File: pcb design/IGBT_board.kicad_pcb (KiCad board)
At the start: 6 copper layers, 200 x 100 mm, 44 parts, among them Q1 IGBT, Q10 IGBT, Q11 IGBT, Q12 IGBT, Q2 IGBT, Q3 IGBT, Q4 IGBT, Q5 IGBT, Q6 IGBT, Q7 IGBT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

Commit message: Draft of bus bars and mounting points
Signed-off-by: Marcos Chaparro <mchaparro@paltatech.com>
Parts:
- MP1: footprint paltatech:heatsink-watercooled-20x210mm -> heatsink-watercooled-20x210mm
- moved R17 360.5 mm to (25.2, -38.8), turned to 90 degrees
- moved R18 340.0 mm to (29.8, -38.8), turned to 90 degrees
- moved R21 336.3 mm to (47.2, -38.8), turned to 90 degrees
- moved R20 333.9 mm to (40.8, -25.2), turned to 270 degrees
- moved R22 333.7 mm to (51.8, -38.8), turned to 90 degrees
- moved R19 332.0 mm to (36.2, -25.2), turned to 270 degrees
- moved R23 315.3 mm to (58.2, -25.2), turned to 270 degrees
- moved R24 301.6 mm to (62.8, -25.2), turned to 270 degrees
- moved R14 190.4 mm to (3.25, -38.8), turned to 90 degrees
- moved R10 183.5 mm to (-14.2, -38.8), turned to 90 degrees
- moved R1 182.1 mm to (-62.8, -38.8), turned to 90 degrees
- moved R6 180.7 mm to (-36.2, -38.8), turned to 90 degrees
- moved R9 180.7 mm to (-18.8, -38.8), turned to 90 degrees
- moved R13 179.4 mm to (7.75, -38.8), turned to 90 degrees
- moved R5 178.0 mm to (-40.8, -38.8), turned to 90 degrees
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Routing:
- net GATE_LOW: track 0.00 -> 140.9 mm
- net (no net): track 110.8 -> 0.00 mm
- net GATE_HIGH: track 98.0 -> 153.7 mm
- net Net-(Q8-Pad1): track 0.00 -> 11.4 mm
- net Net-(Q6-Pad1): track 0.00 -> 11.4 mm
- net Net-(Q4-Pad1): track 0.00 -> 11.4 mm
- net Net-(Q12-Pad1): track 0.00 -> 11.4 mm
- net Net-(Q11-Pad1): track 0.00 -> 11.4 mm
- net Net-(Q10-Pad1): track 0.00 -> 11.4 mm
- net PHASE: track 10.0 -> 0.00 mm
- net VBUS-: track 9.00 -> 0.00 mm
- net Net-(Q3-Pad1): track 3.54 -> 11.4 mm
- net Net-(Q1-Pad1): track 3.54 -> 11.4 mm
- net Net-(Q7-Pad1): track 4.23 -> 11.4 mm
- net Net-(Q9-Pad1): track 4.31 -> 11.4 mm
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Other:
- board size 200 x 100 mm -> 150 x 100 mm

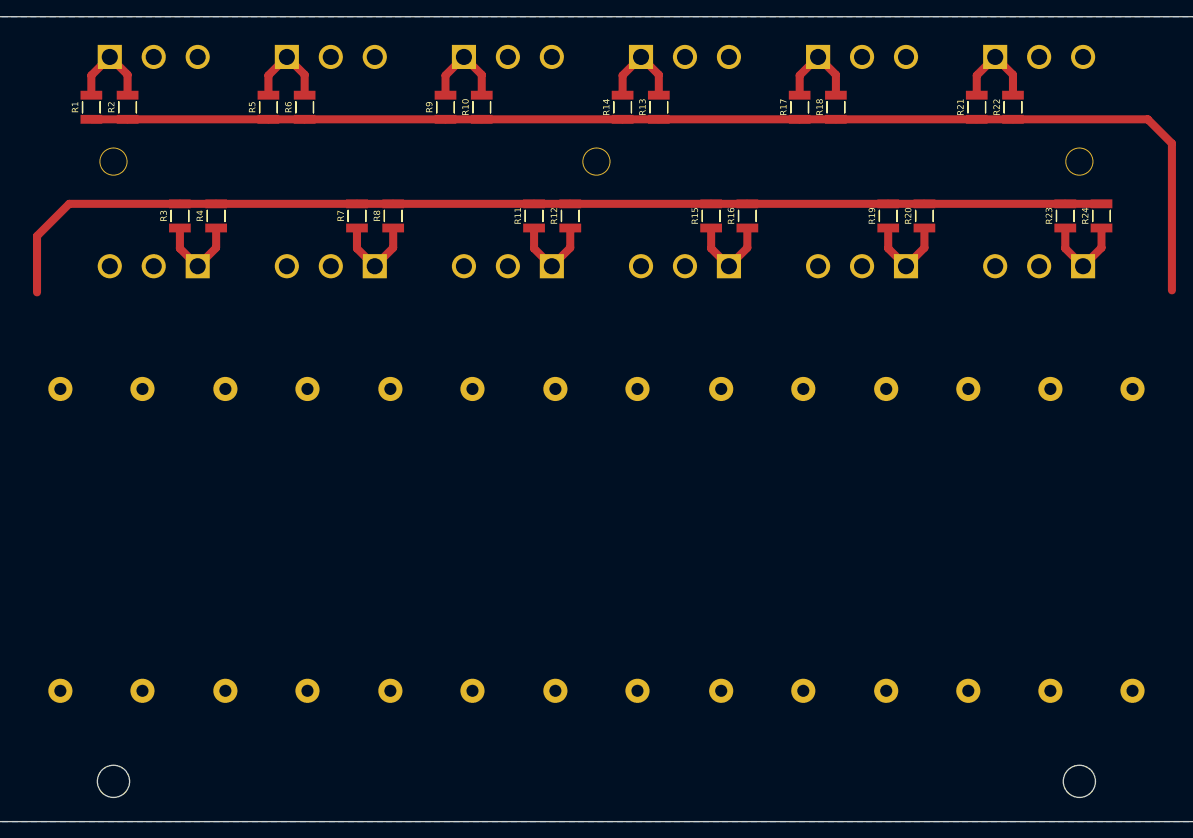
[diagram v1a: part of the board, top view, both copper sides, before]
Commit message: Added IGBT gate driver circuit and isolated power supply
Signed-off-by: Marcos Chaparro <mchaparro@paltatech.com>
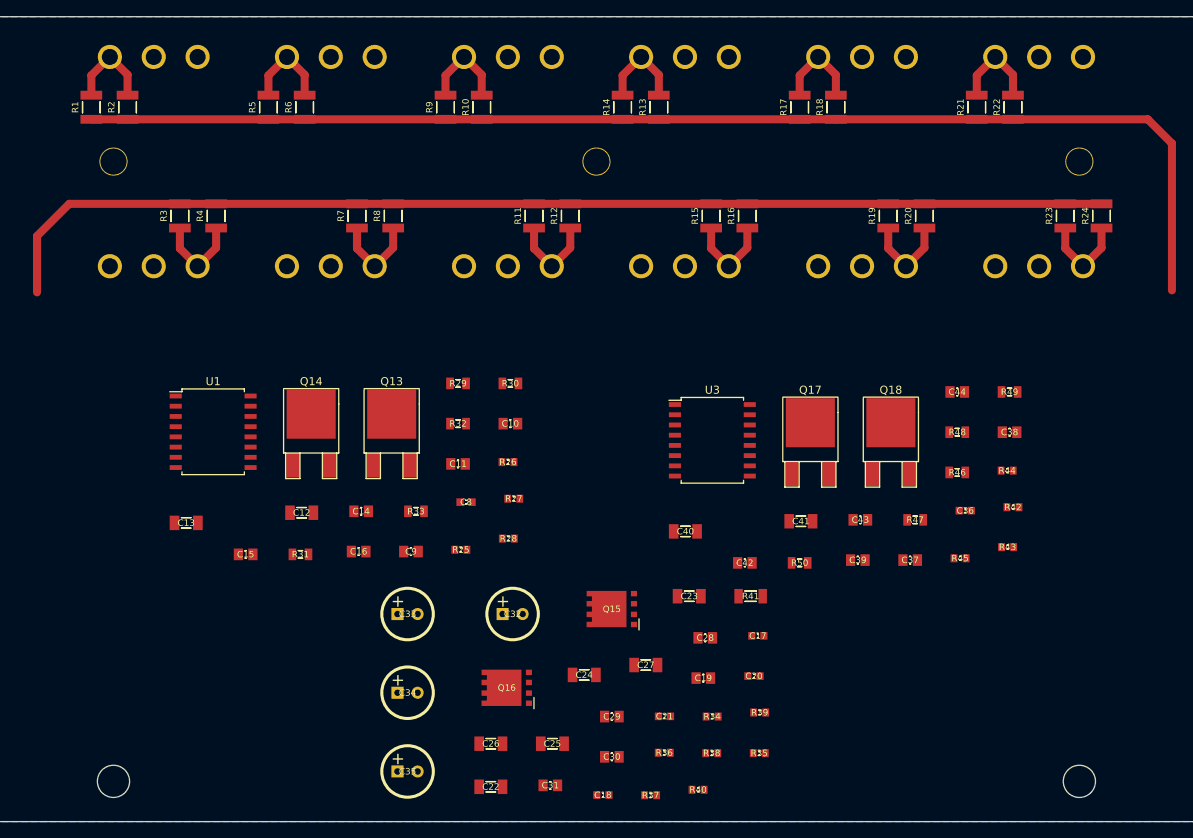
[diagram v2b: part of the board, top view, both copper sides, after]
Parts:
- removed C1, C2, C3, C4, C5, C6, C7: 16uF 700v, paltatech:CAP_FILM_EPCOS_42x20mm
- added C10: 1uF 50v, IPC7351-Nominal:CAPC2012X70, F.Cu at (-10.7, 0.56)
- added C11: 1uF 50v, IPC7351-Nominal:CAPC2012X70, F.Cu at (-17.2, 5.56)
- added C12: 10uF 50v, IPC7351-Nominal:CAPC3216X70, F.Cu at (-36.6, 11.6)
- added C13: 10uF 50v, IPC7351-Nominal:CAPC3216X70, F.Cu at (-51.0, 12.9)
- added C14: 100nF 50v, IPC7351-Nominal:CAPC2012X70, F.Cu at (-29.2, 11.5)
- added C15: 100nF 50v, IPC7351-Nominal:CAPC2012X70, F.Cu at (-43.6, 16.8)
- added C16: 100pF, IPC7351-Nominal:CAPC2012X70, F.Cu at (-29.5, 16.5)
- added C17: 1uF, IPC7351-Nominal:CAPC1608X55, F.Cu at (20.1, 26.9)
- added C18: 22nF, IPC7351-Nominal:CAPC1608X55, F.Cu at (0.80, 46.7)
- added C19: 22uF 16v, IPC7351-Nominal:CAPC2012X70, F.Cu at (13.3, 32.2)
- added C20: 1nF, IPC7351-Nominal:CAPC1608X55, F.Cu at (19.6, 31.9)
- added C21: 470pF, IPC7351-Nominal:CAPC1608X55, F.Cu at (8.45, 36.9)
- added C22: 10uF 50v, IPC7351-Nominal:CAPC3216X70, F.Cu at (-13.1, 45.7)
- added C23: 10uF 50v, IPC7351-Nominal:CAPC3216X70, F.Cu at (11.5, 22.0)
- added C24: 10uF 50v, IPC7351-Nominal:CAPC3216X70, F.Cu at (-1.52, 31.8)
- added C25: 10uF 50v, IPC7351-Nominal:CAPC3216X70, F.Cu at (-5.47, 40.3)
- added C26: 10uF 50v, IPC7351-Nominal:CAPC3216X70, F.Cu at (-13.1, 40.3)
- added C27: 10uF 50v, IPC7351-Nominal:CAPC3216X70, F.Cu at (6.13, 30.5)
- added C28: 100nF 50v, IPC7351-Nominal:CAPC2012X70, F.Cu at (13.5, 27.2)
- added C29: 100nF 50v, IPC7351-Nominal:CAPC2012X70, F.Cu at (1.92, 37.0)
- added C30: 100nF 50v, IPC7351-Nominal:CAPC2012X70, F.Cu at (1.92, 42.0)
- added C31: 100nF 50v, IPC7351-Nominal:CAPC2012X70, F.Cu at (-5.73, 45.5)
- added C32: C-ALUM-6.3mm, pth-passive:C-ALUM-6.3mm, F.Cu at (-10.4, 24.2)
- added C33: C-ALUM-6.3mm, pth-passive:C-ALUM-6.3mm, F.Cu at (-23.5, 24.2)
- added C34: C-ALUM-6.3mm, pth-passive:C-ALUM-6.3mm, F.Cu at (-23.5, 34.0)
- added C35: C-ALUM-6.3mm, pth-passive:C-ALUM-6.3mm, F.Cu at (-23.5, 43.8)
- added C36: 100nF, IPC7351-Nominal:CAPC1608X55, F.Cu at (45.8, 11.4)
- added C37: 1uF 50v, IPC7351-Nominal:CAPC2012X70, F.Cu at (39.0, 17.5)
- added C38: 1uF 50v, IPC7351-Nominal:CAPC2012X70, F.Cu at (51.3, 1.62)
- added C39: 1uF 50v, IPC7351-Nominal:CAPC2012X70, F.Cu at (32.5, 17.5)
- added C40: 10uF 50v, IPC7351-Nominal:CAPC3216X70, F.Cu at (11.1, 13.9)
- added C41: 10uF 50v, IPC7351-Nominal:CAPC3216X70, F.Cu at (25.4, 12.7)
- added C42: 100nF 50v, IPC7351-Nominal:CAPC2012X70, F.Cu at (18.4, 17.9)
- added C43: 100nF 50v, IPC7351-Nominal:CAPC2012X70, F.Cu at (32.8, 12.5)
- added C44: 100pF, IPC7351-Nominal:CAPC2012X70, F.Cu at (44.8, -3.38)
- added C8: 100nF, IPC7351-Nominal:CAPC1608X55, F.Cu at (-16.2, 10.3)
- added C9: 1uF 50v, IPC7351-Nominal:CAPC2012X70, F.Cu at (-23.0, 16.5)
- added Q13: NPN, SMD_Packages:DPAK-2, F.Cu at (-25.4, 5.73)
- added Q14: PNP, SMD_Packages:DPAK-2, F.Cu at (-35.4, 5.73)
- added Q15: CSD19533Q5A, manuf:TEXAS-Q5A, F.Cu at (1.91, 23.6)
- added Q16: CSD19533Q5A, manuf:TEXAS-Q5A, F.Cu at (-11.1, 33.4)
- added Q17: NPN, SMD_Packages:DPAK-2, F.Cu at (26.6, 6.79)
- added Q18: PNP, SMD_Packages:DPAK-2, F.Cu at (36.6, 6.79)
- added R25: 10k, IPC7351-Nominal:RESC1608X50, F.Cu at (-16.8, 16.2)
- added R26: 10k, IPC7351-Nominal:RESC1608X50, F.Cu at (-11.0, 5.34)
- added R27: 10R, IPC7351-Nominal:RESC1608X50, F.Cu at (-10.3, 9.89)
- added R28: 0R, IPC7351-Nominal:RESC1608X50, F.Cu at (-10.9, 14.8)
- added R29: R-0805, IPC7351-Nominal:RESC2012X50, F.Cu at (-17.2, -4.44)
- added R30: R-0805, IPC7351-Nominal:RESC2012X50, F.Cu at (-10.7, -4.44)
- added R31: 10R, IPC7351-Nominal:RESC2012X50, F.Cu at (-36.8, 16.8)
- added R32: 0R, IPC7351-Nominal:RESC2012X50, F.Cu at (-17.2, 0.56)
- added R33: 1k, IPC7351-Nominal:RESC2012X50, F.Cu at (-22.4, 11.5)
- added R34: 0R, IPC7351-Nominal:RESC1608X50, F.Cu at (14.4, 36.9)
- added R35: 26.7k, IPC7351-Nominal:RESC1608X50, F.Cu at (20.2, 41.5)
- added R36: 1k, IPC7351-Nominal:RESC1608X50, F.Cu at (8.43, 41.4)
- added R37: 0R, IPC7351-Nominal:RESC1608X50, F.Cu at (6.73, 46.7)
- added R38: 22R, IPC7351-Nominal:RESC1608X50, F.Cu at (14.3, 41.5)
- added R39: 22R, IPC7351-Nominal:RESC1608X50, F.Cu at (20.3, 36.4)
- added R40: 1.15k, IPC7351-Nominal:RESC1608X50, F.Cu at (12.6, 46.0)
- added R41: 0.22R, IPC7351-Nominal:RESC3216X60, F.Cu at (19.2, 22.0)
- added R42: 10k, IPC7351-Nominal:RESC1608X50, F.Cu at (51.7, 10.9)
- added R43: 10k, IPC7351-Nominal:RESC1608X50, F.Cu at (51.1, 15.9)
- added R44: 10R, IPC7351-Nominal:RESC1608X50, F.Cu at (51.0, 6.40)
- added R45: 0R, IPC7351-Nominal:RESC1608X50, F.Cu at (45.2, 17.3)
- added R46: R-0805, IPC7351-Nominal:RESC2012X50, F.Cu at (44.8, 6.62)
- added R47: R-0805, IPC7351-Nominal:RESC2012X50, F.Cu at (39.6, 12.5)
- added R48: 10R, IPC7351-Nominal:RESC2012X50, F.Cu at (44.8, 1.62)
- added R49: 0R, IPC7351-Nominal:RESC2012X50, F.Cu at (51.3, -3.38)
- added R50: 1k, IPC7351-Nominal:RESC2012X50, F.Cu at (25.2, 17.9)
- added U1: ISO5852S, Housings_SOIC:SOIC-16_7.5x10.3mm_Pitch1.27mm, F.Cu at (-47.6, 1.57)
- added U3: ISO5852S, Housings_SOIC:SOIC-16_7.5x10.3mm_Pitch1.27mm, F.Cu at (14.4, 2.63)
- MP1: footprint heatsink-watercooled-20x210mm -> paltatech:heatsink-watercooled-20x210mm
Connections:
- Q10 pad 3: VBUS- -> PHASE
- Q12 pad 3: VBUS- -> PHASE
- Q2 pad 3: VBUS- -> PHASE
- Q4 pad 3: VBUS- -> PHASE
- Q6 pad 3: VBUS- -> PHASE
- Q8 pad 3: VBUS- -> PHASE

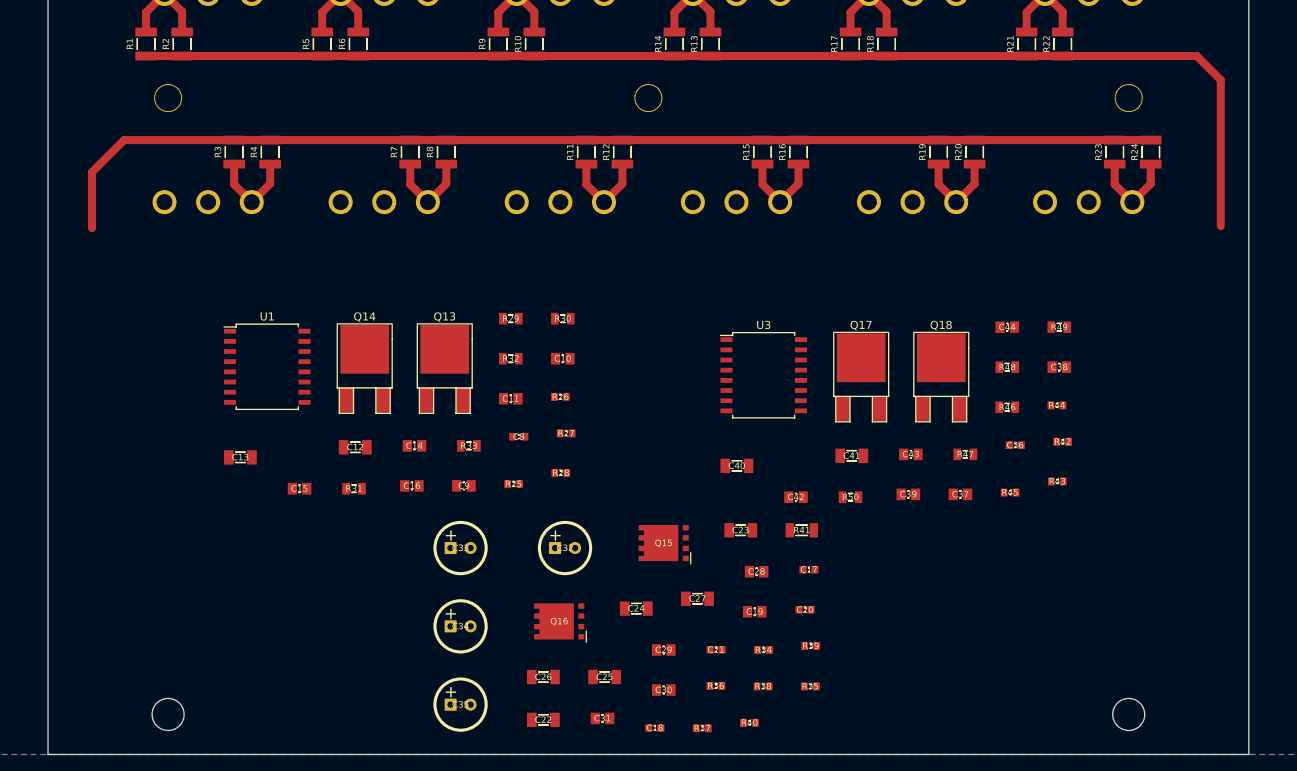
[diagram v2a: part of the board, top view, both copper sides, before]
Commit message: Add footprints, more layout and graphics
Signed-off-by: Marcos Chaparro <mchaparro@paltatech.com>
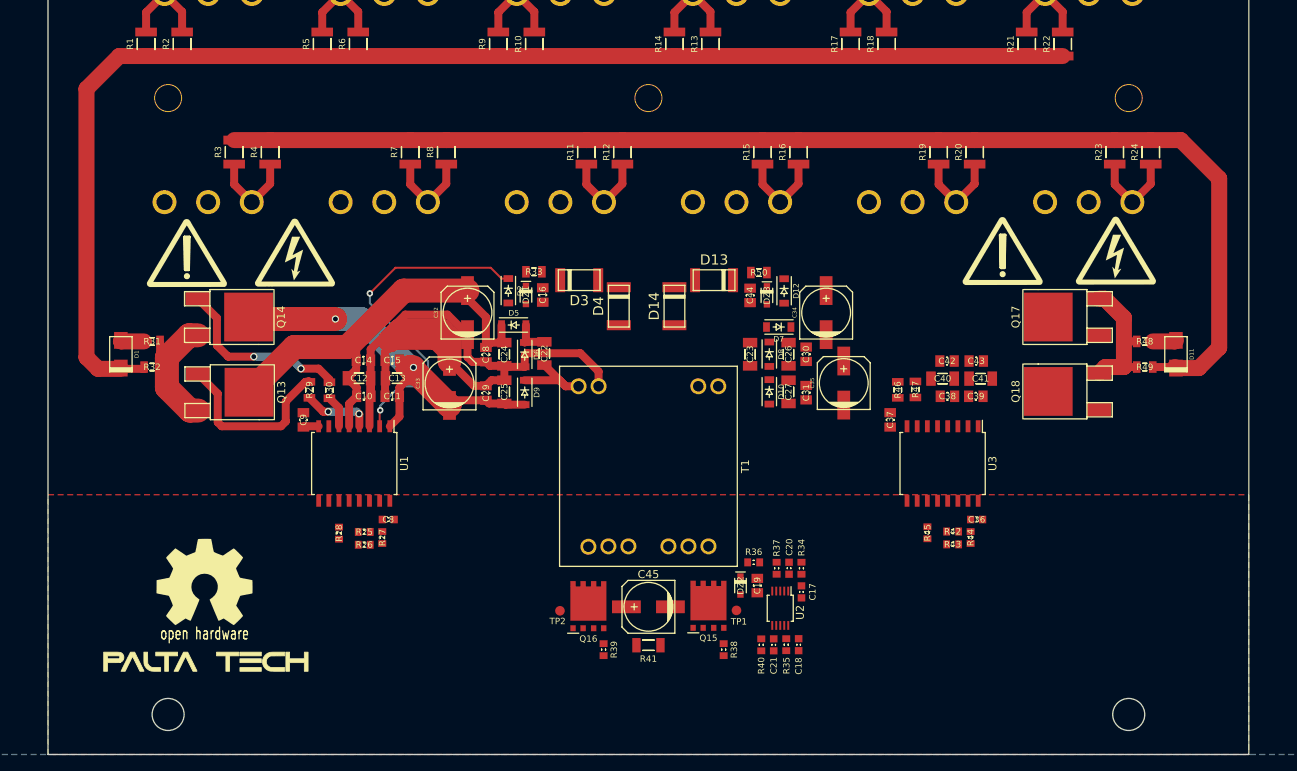
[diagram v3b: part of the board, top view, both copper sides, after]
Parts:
- added C45: 47uF 50v, w_smd_cap:c_elec_6.3x7.7, F.Cu at (0.00, 31.6)
- added D1: SK310A-LTP, w_smd_diode:do214ac, F.Cu at (-65.9, 0.00)
- added D10: RB160MM-60TR, paltatech:SOD-123F, F.Cu at (15.1, 4.70)
- added D11: SK310A-LTP, w_smd_diode:do214ac, F.Cu at (65.9, 0.00)
- added D12: RB160MM-60TR, paltatech:SOD-123F, F.Cu at (16.9, -7.90)
- added D13: GL41Y-E3/96, paltatech:melf-DO-213AB, F.Cu at (8.20, -9.25)
- added D14: GL41Y-E3/96, paltatech:melf-DO-213AB, F.Cu at (3.25, -6.00)
- added D2: RB160MM-60TR, paltatech:SOD-123F, F.Cu at (-17.5, -7.92)
- added D3: GL41Y-E3/96, paltatech:melf-DO-213AB, F.Cu at (-8.65, -9.25)
- added D4: GL41Y-E3/96, paltatech:melf-DO-213AB, F.Cu at (-3.70, -6.00)
- added D5: RB160MM-60TR, paltatech:SOD-123F, F.Cu at (-16.8, -3.65)
- added D6: RB160MM-60TR, paltatech:SOD-123F, F.Cu at (-15.4, 0.05)
- added D7: RB160MM-60TR, paltatech:SOD-123F, F.Cu at (16.3, -3.40)
- added D8: RB160MM-60TR, paltatech:SOD-123F, F.Cu at (15.1, 0.00)
- added D9: RB160MM-60TR, paltatech:SOD-123F, F.Cu at (-15.4, 4.78)
- added DZ1: MM3Z12VB, smd-semi:SOD-323F, F.Cu at (-15.3, -7.40)
- added DZ2: 12v zener, smd-semi:SOD-323F, F.Cu at (11.5, 28.9)
- added DZ3: MM3Z12VB, smd-semi:SOD-323F, F.Cu at (14.8, -7.35)
- added G***: LOGO, paltatech:PALTA_TECH_SILKS_26mm, F.Cu at (-55.5, 38.4)
- added G***: LOGO, w_logo:Logo_silk_OSHW_12x13mm, F.Cu at (-55.5, 28.4)
- added G***: LOGO, w_logo:Logo_silk_warning_10x8.5mm, F.Cu at (44.2, -12.9)
- added G***: LOGO, w_logo:Logo_silk_high_voltage_10x8.5mm, F.Cu at (58.4, -12.9)
- added G***: LOGO, w_logo:Logo_silk_high_voltage_10x8.5mm, F.Cu at (-44.1, -12.7)
- added G***: LOGO, w_logo:Logo_silk_warning_10x8.5mm, F.Cu at (-57.6, -12.7)
- added T1: TRANS-3-1CT, paltatech:wurth_750342312, F.Cu at (0.00, 14.0)
- added TP1: TESTPOINT, conn-test:TEST-SMD-SMALL, F.Cu at (11.0, 32.0)
- added TP2: TESTPOINT, conn-test:TEST-SMD-SMALL, F.Cu at (-11.1, 32.0)
- added U2: LM5030, TSSOP-10_3x3mm_Pitch0.5mm, F.Cu at (16.5, 31.7)
- C32, C33, C34, C35: value C-ALUM-6.3mm -> 47uF 50v; footprint pth-passive:C-ALUM-6.3mm -> w_smd_cap:c_elec_6.3x7.7
- R36: value 1k -> 1.15k
- moved C35 62.5 mm to (24.4, 3.60), turned to 90 degrees
- moved C34 60.2 mm to (22.2, -5.20), turned to 90 degrees
- moved C26 50.6 mm to (17.5, 0.00), turned to 270 degrees
- moved C31 48.0 mm to (19.7, 4.80), turned to 270 degrees
- moved C22 45.8 mm to (-13.0, -0.10), turned to 270 degrees
- moved C30 45.6 mm to (19.7, 0.00), turned to 270 degrees
- moved R32 44.8 mm to (-62.0, 1.60)
- moved C28 43.3 mm to (-20.3, 0.05), turned to 270 degrees
- moved C29 39.0 mm to (-20.3, 4.85), turned to 270 degrees
- moved C25 37.8 mm to (-18.0, 4.70), turned to 270 degrees
- moved C24 35.8 mm to (-18.0, 0.00), turned to 270 degrees
- moved C44 32.4 mm to (12.7, -7.35), turned to 270 degrees
- moved Q17 31.8 mm to (56.3, -4.65), turned to 90 degrees
- moved C32 31.8 mm to (-22.6, -5.20), turned to 90 degrees
- moved R31 31.2 mm to (-62.0, -1.60)
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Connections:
- C17 pad 1: PHASE -> GND
- C18 pad 1: PHASE -> GND
- C19 pad 2: PHASE -> GND
- C20 pad 2: PHASE -> GND
- C21 pad 2: PHASE -> GND
- C26 pad 2: PHASE -> VBUS-
- C27 pad 1: PHASE -> VBUS-
- C30 pad 2: PHASE -> VBUS-
- C31 pad 1: PHASE -> VBUS-
- C34 pad 2: PHASE -> VBUS-
- C35 pad 1: PHASE -> VBUS-
- C36 pad 2: PHASE -> GND
- C37 pad 1: PHASE -> VBUS-
- C38 pad 2: PHASE -> VBUS-
- C39 pad 1: PHASE -> VBUS-
- C40 pad 2: PHASE -> VBUS-
- C41 pad 1: PHASE -> VBUS-
- C42 pad 2: PHASE -> VBUS-
- C43 pad 1: PHASE -> VBUS-
- C44 pad 2: PHASE -> VBUS-
- C8 pad 2: PHASE -> GND
- Q10 pad 3: PHASE -> VBUS-
- Q12 pad 3: PHASE -> VBUS-
- Q2 pad 3: PHASE -> VBUS-
- Q4 pad 3: PHASE -> VBUS-
- Q6 pad 3: PHASE -> VBUS-
- Q8 pad 3: PHASE -> VBUS-
- R28 pad 1: PHASE -> GND
- R35 pad 2: PHASE -> GND
- R41 pad 2: PHASE -> GND
- R45 pad 1: PHASE -> GND
- U1 pad 16: PHASE -> GND
- U1 pad 9: PHASE -> GND
- U3 pad 16: PHASE -> GND
- U3 pad 3: PHASE -> VBUS-
- U3 pad 9: PHASE -> GND
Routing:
- net PHASE: track 0.00 -> 87.2 mm
- net /IGBT_driver_TOP/+15V: track 0.00 -> 61.8 mm
- net /IGBT_driver_TOP/-8V: track 0.00 -> 61.3 mm, vias 0 -> 2
- net Net-(C16-Pad1): track 0.00 -> 42.7 mm, vias 0 -> 2
- net Net-(Q17-Pad3): track 0.00 -> 28.7 mm
- net Net-(Q14-Pad1): track 0.00 -> 23.0 mm, vias 0 -> 2
- net Net-(Q13-Pad1): track 0.00 -> 22.8 mm
- net Net-(Q13-Pad3): track 0.00 -> 19.1 mm
- net GATE_LOW: track 140.9 -> 155.6 mm
- net GATE_HIGH: track 153.7 -> 165.0 mm
- net Net-(C22-Pad2): track 0.00 -> 10.8 mm
- net Net-(R29-Pad2): track 0.00 -> 8.59 mm, vias 0 -> 2
- net Net-(C22-Pad1): track 0.00 -> 4.72 mm
- net Net-(R30-Pad2): track 0.00 -> 3.99 mm
- net Net-(D11-Pad1): track 0.00 -> 2.95 mm
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- added copper zone on F.Cu, net GND
